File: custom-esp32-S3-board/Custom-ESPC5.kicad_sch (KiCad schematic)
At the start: 52 parts, among them J1 Screw_Terminal_01x02, J10 Barrel_Jack, J12 Conn_01x05, J13 Conn_01x05, J4 USB_C_Receptacle_USB2.0_14P, J5 Conn_01x03, J6 Screw_Terminal_01x03, SW1 SW_Nidec_CAS-120A1, SW2 SW_Push, SW3 SW_Push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

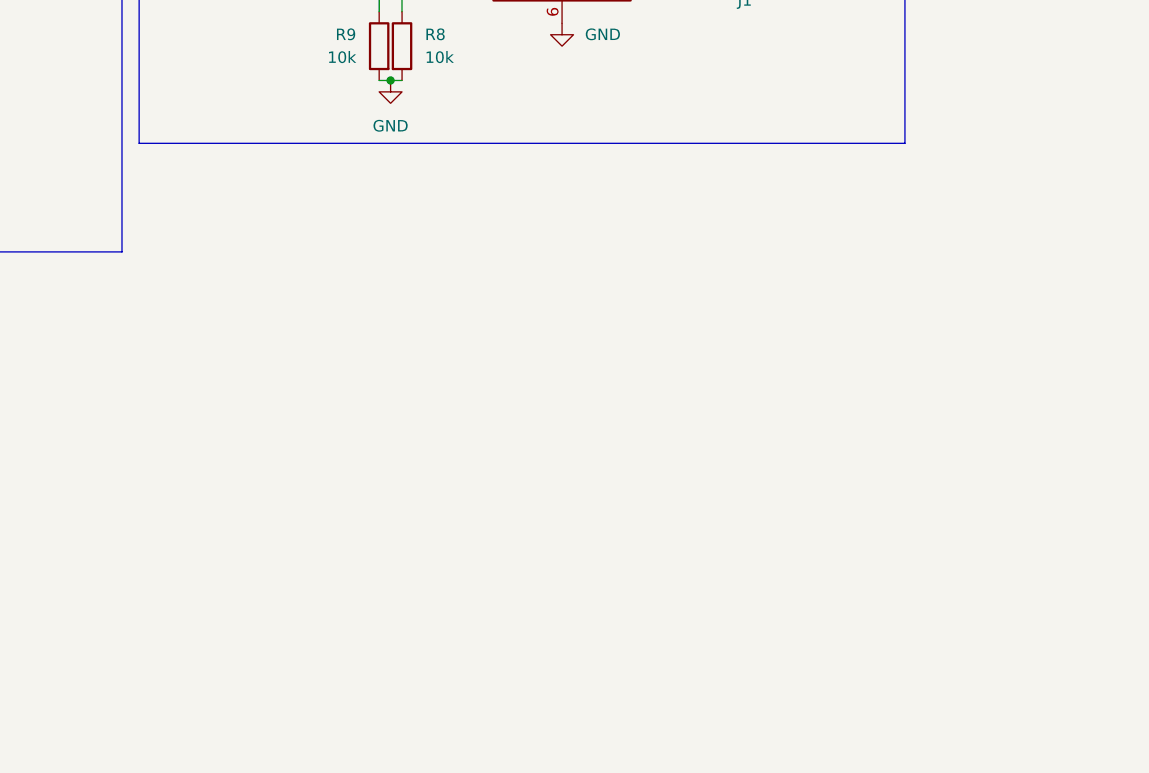
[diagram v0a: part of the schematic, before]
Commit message: add auto-reset
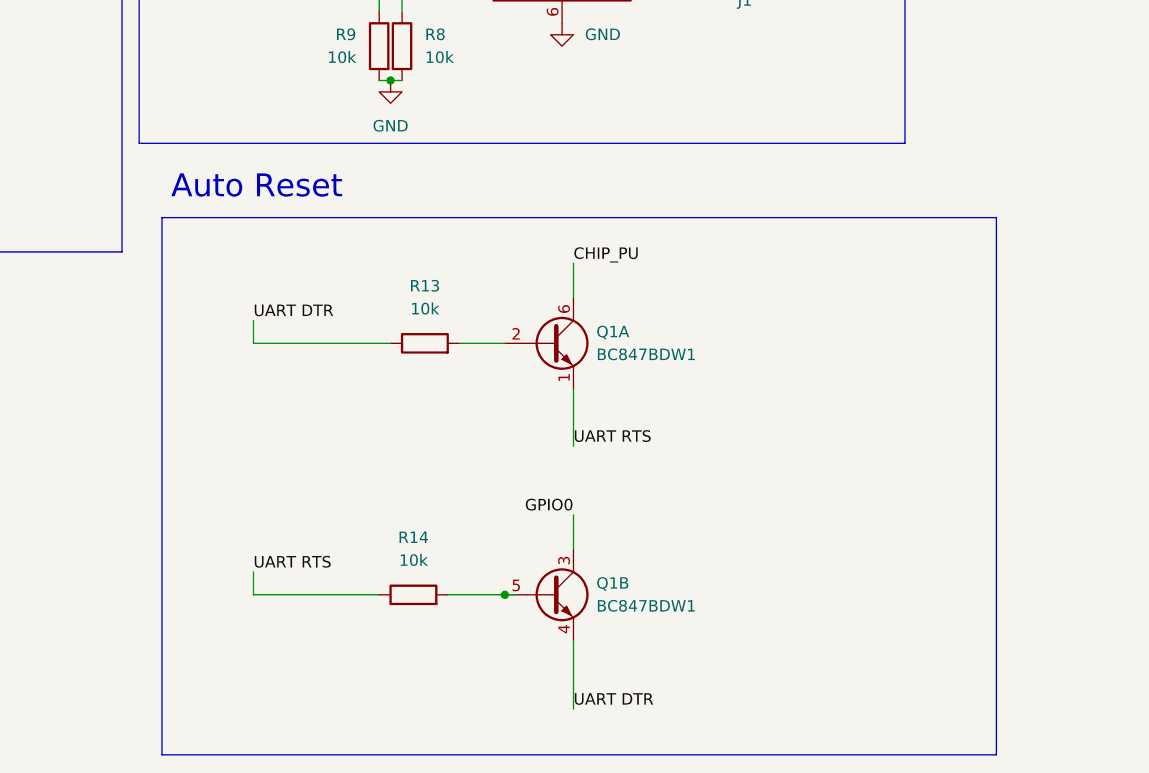
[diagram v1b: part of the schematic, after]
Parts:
- added Q1: BC847BDW1, Package_TO_SOT_SMD:SOT-363_SC-70-6, symbol Transistor_BJT:BC847BDW1
- added R13, R14: 10k, symbol Device:R
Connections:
- net CHIP_PU: now also Q1.6 (C1)
- net GPIO0: now also Q1.3 (C2)
- net UART DTR: now also Q1.4 (E2), R13.1
- net UART RTS: now also Q1.1 (E1), R14.1
- new net: Q1.5 (B2), R14.2
- new net: Q1.2 (B1), R13.2
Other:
- note added: "Auto Reset"

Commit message: Finalize Schematic
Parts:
- removed D1, D4: D, Diode_SMD:USC-TOS, symbol Device:D
- added C17, C18, C19, C20: 0.1u, Capacitor_SMD:C_0402_1005Metric, symbol Device:C
- added J2, J3, J7, J8: Conn_01x02_Pin, Connector_PinHeader_2.54mm:PinHeader_1x02_P2.54mm_Vertical, symbol Connector:Conn_01x02_Pin
- R13, R14: footprint (none) -> Resistor_SMD:R_0402_1005Metric
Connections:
- net +3.3V: no longer J5.1 (Pin_1)
- net +5V: now also J7.1 (Pin_1), J8.2 (Pin_2)
- net A1: now also C19.1
- net A2: now also C17.1
- net B1: now also C20.1
- net B2: now also C18.1
- net CHIP_PU: now also J2.1 (Pin_1); no longer Q1.6 (C1)
- net GND: now also C17.2, C18.2, C19.2, C20.2
- net GPIO0: now also J3.1 (Pin_1); no longer Q1.3 (C2)
- net at C5.1, C6.1, D2.2 (K)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: now also J7.2 (Pin_2)
- net at C2.1, R2.2, U2.2 (VO): now also J8.1 (Pin_1)
- net UART1 RX: now reaches U6.11 (IO18)
- net UART RX renamed UART0 RX
- net UART TX renamed UART0 TX
- net WS2812 renamed UART1 TX
- net UART1 TX: no longer J5.2 (Pin_2)
- new net: J3.2 (Pin_2), Q1.3 (C2)
- new net: J2.2 (Pin_2), Q1.6 (C1)
- new net UART1_RX: J5.2 (Pin_2)
- new net UART1_TX: J5.1 (Pin_1)
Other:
- note added: "Hall Effect Sensor Decoupling Caps"
- note added: "PDH Power Select"
- note added: "Shunt"
- note added: "UART JST"
- note added: "USB Power Select"
- note removed: "Forward voltage drop: 0.1 V @ 10mA 0.22V @ 100 mA 0.34 V @ 1 A"
- note removed: "WS2812 LEDs"
- moved on the sheet: Q1A, Q1B, R13, R14

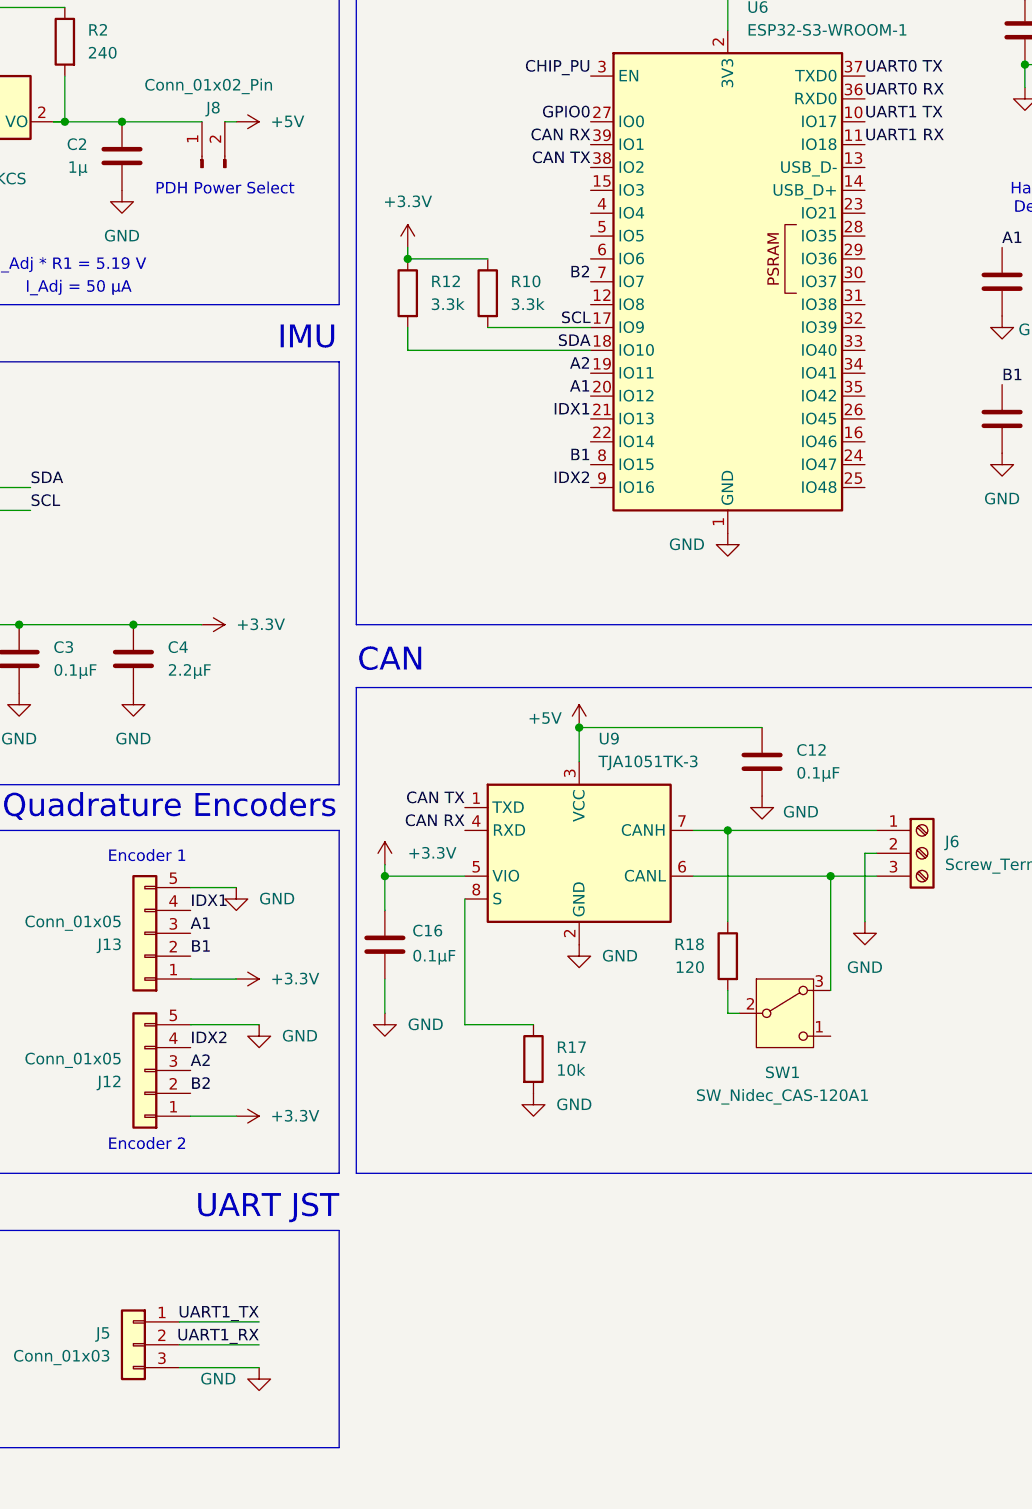
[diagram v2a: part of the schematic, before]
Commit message: Fix pin labels in schematic
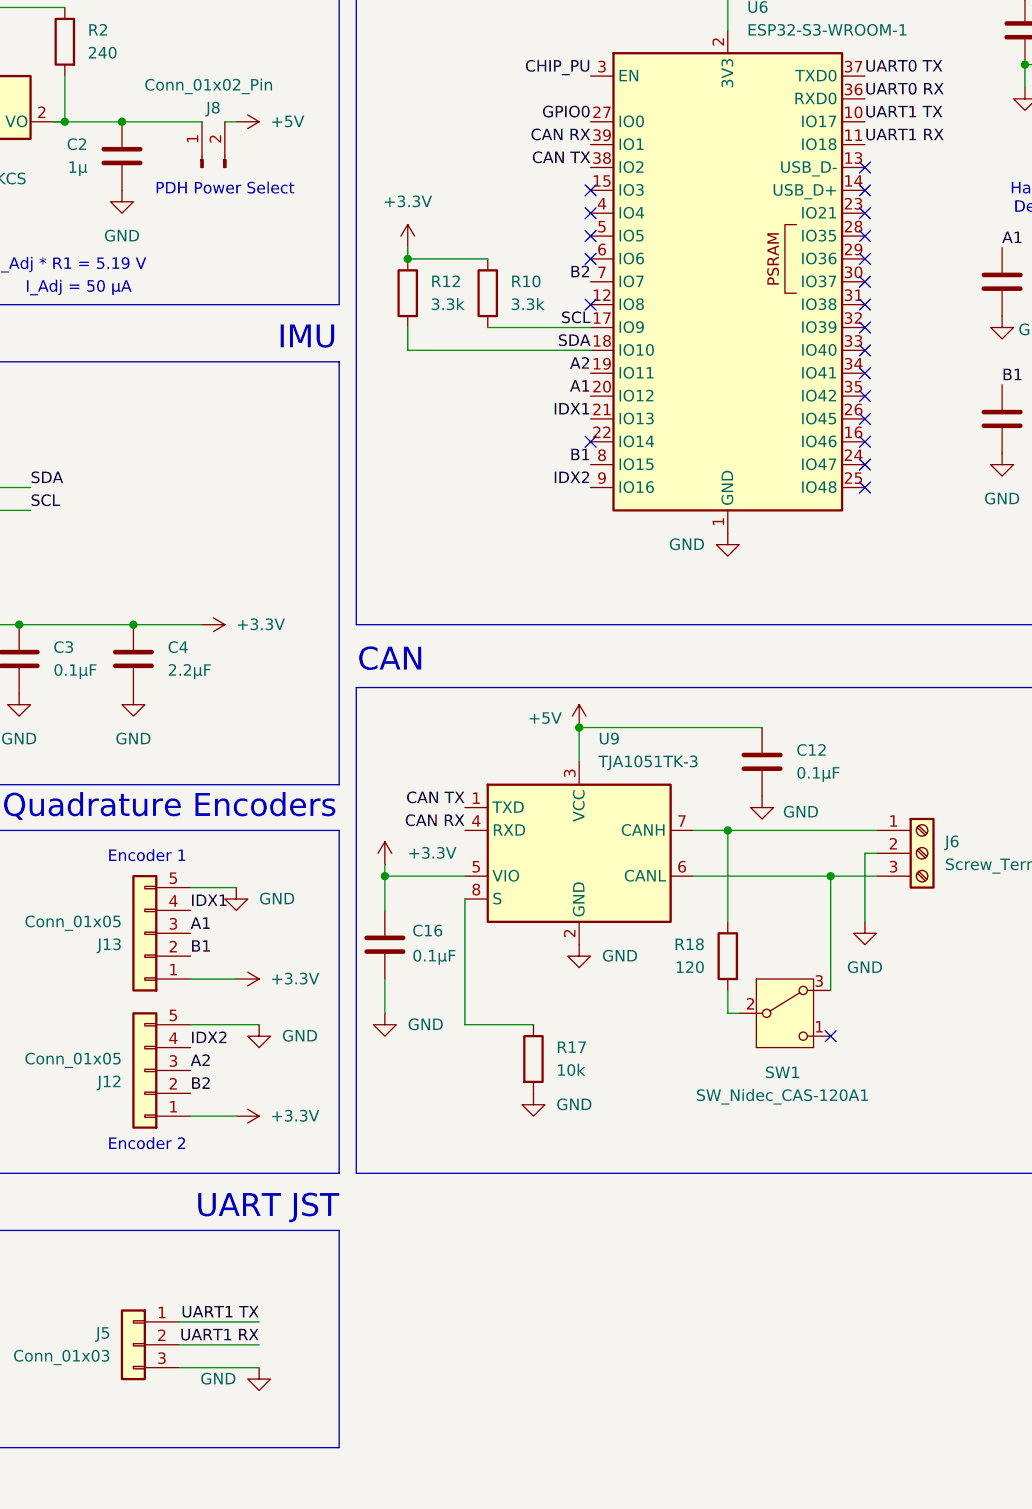
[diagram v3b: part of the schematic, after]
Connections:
- net UART1_RX is gone; now on net UART1 RX: J5.2 (Pin_2)
- net UART1_TX is gone; now on net UART1 TX: J5.1 (Pin_1)
- no-connect marks 16 -> 38
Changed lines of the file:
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@@
+	)
+	(no_connect
+		(at 596.9 387.35)
+	)
+	(no_connect
+		(at 596.9 356.87)
 	)
 	(no_connect
@@
 	)
 	(no_connect
+		(at 596.9 382.27)
+	)
+	(no_connect
 		(at 727.71 351.79)
 	)
 	(no_connect
+		(at 593.09 450.85)
+	)
+	(no_connect
+		(at 596.9 369.57)
+	)
+	(no_connect
+		(at 596.9 389.89)
+	)
+	(no_connect
 		(at 727.71 349.25)
 	)
 	(no_connect
+		(at 596.9 359.41)
+	)
+	(no_connect
+		(at 566.42 384.81)
+	)
+	(no_connect
 		(at 727.71 356.87)
 	)
@@
 	)
 	(no_connect
+		(at 596.9 364.49)
+	)
+	(no_connect
+		(at 566.42 369.57)
+	)
+	(no_connect
+		(at 566.42 356.87)
+	)
+	(no_connect
 		(at 727.71 359.41)
 	)
@@
 	)
 	(no_connect
+		(at 596.9 379.73)
+	)
+	(no_connect
+		(at 566.42 364.49)
+	)
+	(no_connect
+		(at 596.9 361.95)
+	)
+	(no_connect
+		(at 596.9 372.11)
+	)
+	(no_connect
 		(at 402.59 397.51)
 	)
 	(no_connect
+		(at 596.9 374.65)
+	)
+	(no_connect
 		(at 727.71 364.49)
 	)
 	(no_connect
+		(at 566.42 361.95)
+	)
+	(no_connect
 		(at 727.71 334.01)
 	)
 	(no_connect
 		(at 650.24 384.81)
+	)
+	(no_connect
+		(at 596.9 384.81)
+	)
+	(no_connect
+		(at 566.42 359.41)
+	)
+	(no_connect
+		(at 596.9 367.03)
+	)
+	(no_connect
+		(at 596.9 354.33)
+	)
+	(no_connect
+		(at 596.9 377.19)
 	)
 	(no_connect
@@
 		)
 	)
-	(label "UART1_TX"
+	(label "UART1 TX"
 		(at 529.59 482.6 180)
 		(effects
@@
 		)
 	)
-	(label "UART1_RX"
+	(label "UART1 RX"
 		(at 529.59 485.14 180)
 		(effects

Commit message: Finish routing for subcircuits
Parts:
- added H1, H2, H3: MountingHole, MountingHole:MountingHole_4.5mm, symbol Mechanical:MountingHole
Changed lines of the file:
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@@
 	)
 	(symbol
+		(lib_id "Mechanical:MountingHole")
+		(at 586.74 490.22 0)
+		(unit 1)
+		(exclude_from_sim no)
+		(in_bom no)
+		(on_board yes)
+		(dnp no)
+		(fields_autoplaced yes)
+		(property "Reference" "H2"
+			(at 589.28 488.9499 0)
+			(effects
+				(font
+					(size 1.27 1.27)
+				)
+				(justify left)
+			)
+		)
+		(property "Value" "MountingHole"
+			(at 589.28 491.4899 0)
+			(effects
+				(font
+					(size 1.27 1.27)
+				)
+				(justify left)
+			)
+		)
+		(property "Footprint" "MountingHole:MountingHole_4.5mm"
+			(at 586.74 490.22 0)
+			(effects
+				(font
+					(size 1.27 1.27)
+				)
+				(hide yes)
+			)
+		)
+		(property "Datasheet" "~"
+			(at 586.74 490.22 0)
+			(effects
+				(font
+					(size 1.27 1.27)
+				)
+				(hide yes)
+			)
+		)
+		(property "Description" "Mounting Hole without connection"
+			(at 586.74 490.22 0)
+			(effects
+				(font
+					(size 1.27 1.27)
+				)
+				(hide yes)
+			)
+		)
+		(instances
+			(project "Custom-ESPC5"
+				(path "/7f255074-3667-433c-aa2e-2c052ef2e2c8"
+					(reference "H2")
+					(unit 1)
+				)
+			)
+		)
+	)
+	(symbol
 		(lib_id "Device:C")
 		(at 585.47 420.37 0)
@@
 	)
 	(symbol
+		(lib_id "Mechanical:MountingHole")
+		(at 562.61 506.73 0)
+		(unit 1)
+		(exclude_from_sim no)
+		(in_bom no)
+		(on_board yes)
+		(dnp no)
+		(fields_autoplaced yes)
+		(property "Reference" "H3"
+			(at 565.15 505.4599 0)
+			(effects
+				(font
+					(size 1.27 1.27)
+				)
+				(justify left)
+			)
+		)
+		(property "Value" "MountingHole"
+			(at 565.15 507.9999 0)
+			(effects
+				(font
+					(size 1.27 1.27)
+				)
+				(justify left)
+			)
+		)
+		(property "Footprint" "MountingHole:MountingHole_4.5mm"
+			(at 562.61 506.73 0)
+			(effects
+				(font
+					(size 1.27 1.27)
+				)
+				(hide yes)
+			)
+		)
+		(property "Datasheet" "~"
+			(at 562.61 506.73 0)
+			(effects
+				(font
+					(size 1.27 1.27)
+				)
+				(hide yes)
+			)
+		)
+		(property "Description" "Mounting Hole without connection"
+			(at 562.61 506.73 0)
+			(effects
+				(font
+					(size 1.27 1.27)
+				)
+				(hide yes)
+			)
+		)
+		(instances
+			(project "Custom-ESPC5"
+				(path "/7f255074-3667-433c-aa2e-2c052ef2e2c8"
+					(reference "H3")
+					(unit 1)
+				)
+			)
+		)
+	)
+	(symbol
 		(lib_id "Regulator_Linear:LM3940")
 		(at 609.6 297.18 0)
@@
 					(unit 1)
 				)
+			)
+		)
+	)
+	(symbol
+		(lib_id "Mechanical:MountingHole")
+		(at 562.61 490.22 0)
+		(unit 1)
+		(exclude_from_sim no)
+		(in_bom no)
+		(on_board yes)
+		(dnp no)
+		(fields_autoplaced yes)
+		(property "Reference" "H1"
+			(at 565.15 488.9499 0)
+			(effects
+				(font
+					(size 1.27 1.27)
+				)
+				(justify left)
+			)
+		)
+		(property "Value" "MountingHole"
+			(at 565.15 491.4899 0)
+			(effects
+				(font
+					(size 1.27 1.27)
+				)
+				(justify left)
+			)
+		)
+		(property "Footprint" "MountingHole:MountingHole_4.5mm"
+			(at 562.61 490.22 0)
+			(effects
+				(font
+					(size 1.27 1.27)
+				)
+				(hide yes)
+			)
+		)
+		(property "Datasheet" "~"
+			(at 562.61 490.22 0)
+			(effects
+				(font
+					(size 1.27 1.27)
+				)
+				(hide yes)
+			)
+		)
+		(property "Description" "Mounting Hole without connection"
+			(at 562.61 490.22 0)
+			(effects
+				(font
+					(size 1.27 1.27)
+				)
+				(hide yes)
+			)
+		)
+		(instances
+			(project ""
+				(path "/7f255074-3667-433c-aa2e-2c052ef2e2c8"
+					(reference "H1")
+					(unit 1)
+				)

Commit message: Final Edits
Generated gerbers
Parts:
- removed R11, R16: 10k, Resistor_SMD:R_0402_1005Metric, symbol Device:R
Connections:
- net CHIP_PU: now also SW2.2
- net GND: no longer J1.2 (Pin_2), U5.7 (IN-)
- net GPIO0: now also SW3.2
- new net: J1.2 (Pin_2), U5.7 (IN-)
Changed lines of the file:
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@@
 	)
 	(junction
-		(at 689.61 433.07)
-		(diameter 0)
-		(color 0 0 0 0)
-	)
-	(junction
 		(at 678.18 420.37)
 		(diameter 0)
@@
 	(wire
 		(pts
-			(xy 574.04 304.8) (xy 574.04 303.53)
-		)
-		(stroke
-			(width 0)
-			(type default)
-		)
-	)
-	(wire
-		(pts
 			(xy 499.11 325.12) (xy 499.11 327.66)
 		)
@@
 	(wire
 		(pts
+			(xy 574.04 303.53) (xy 574.04 313.69)
+		)
+		(stroke
+			(width 0)
+			(type default)
+		)
+	)
+	(wire
+		(pts
 			(xy 654.685 330.2) (xy 654.685 328.93)
 		)
@@
 	(wire
 		(pts
-			(xy 515.62 304.8) (xy 511.81 304.8)
+			(xy 511.81 304.8) (xy 523.24 304.8)
 		)
 		(stroke
@@
 	(wire
 		(pts
-			(xy 689.61 433.07) (xy 688.34 433.07)
-		)
-		(stroke
-			(width 0)
-			(type default)
-		)
-	)
-	(wire
-		(pts
 			(xy 673.1 364.49) (xy 680.72 364.49)
 		)
@@
 	(wire
 		(pts
-			(xy 690.88 433.07) (xy 689.61 433.07)
+			(xy 688.34 433.07) (xy 690.88 433.07)
 		)
 		(stroke
@@
 	(wire
 		(pts
-			(xy 574.04 313.69) (xy 574.04 312.42)
-		)
-		(stroke
-			(width 0)
-			(type default)
-		)
-	)
-	(wire
-		(pts
 			(xy 693.42 431.8) (xy 690.88 431.8)
 		)
@@
 	)
 	(symbol
-		(lib_id "power:GND")
-		(at 689.61 433.07 0)
-		(unit 1)
-		(exclude_from_sim no)
-		(in_bom yes)
-		(on_board yes)
-		(dnp no)
-		(property "Reference" "#PWR026"
-			(at 689.61 439.42 0)
-			(effects
-				(font
-					(size 1.27 1.27)
-				)
-				(hide yes)
-			)
-		)
-		(property "Value" "GND"
-			(at 687.578 436.88 0)
-			(effects
-				(font
-					(size 1.27 1.27)
-				)
-				(justify left)
-			)
-		)
-		(property "Footprint" ""
-			(at 689.61 433.07 0)
-			(effects
-				(font
-					(size 1.27 1.27)
-				)
-				(hide yes)
-			)
-		)
-		(property "Datasheet" ""
-			(at 689.61 433.07 0)
-			(effects
-				(font
-					(size 1.27 1.27)
-				)
-				(hide yes)
-			)
-		)
-		(property "Description" "Power symbol creates a global label with name \"GND\" , ground"
-			(at 689.61 433.07 0)
-			(effects
-				(font
-					(size 1.27 1.27)
-				)
-				(hide yes)
-			)
-		)
-		(pin "1"
-		)
-		(instances
-			(project "Custom-ESPC5"
-				(path "/7f255074-3667-433c-aa2e-2c052ef2e2c8"
-					(reference "#PWR026")
-					(unit 1)
-				)
-			)
-		)
-	)
-	(symbol
 		(lib_id "Connector:Barrel_Jack")
 		(at 468.63 346.71 0)
@@
 	)
 	(symbol
-		(lib_id "Device:R")
-		(at 574.04 308.61 0)
-		(unit 1)
-		(exclude_from_sim no)
-		(in_bom yes)
-		(on_board yes)
-		(dnp no)
-		(fields_autoplaced yes)
-		(property "Reference" "R16"
-			(at 576.58 307.3399 0)
-			(effects
-				(font
-					(size 1.27 1.27)
-				)
-				(justify left)
-			)
-		)
-		(property "Value" "10k"
-			(at 576.58 309.8799 0)
-			(effects
-				(font
-					(size 1.27 1.27)
-				)
-				(justify left)
-			)
-		)
-		(property "Footprint" "Resistor_SMD:R_0402_1005Metric"
-			(at 572.262 308.61 90)
-			(effects
-				(font
-					(size 1.27 1.27)
-				)
-				(hide yes)
-			)
-		)
-		(property "Datasheet" "~"
-			(at 574.04 308.61 0)
-			(effects
-				(font
-					(size 1.27 1.27)
-				)
-				(hide yes)
-			)
-		)
-		(property "Description" "Resistor"
-			(at 574.04 308.61 0)
-			(effects
-				(font
-					(size 1.27 1.27)
-				)
-				(hide yes)
-			)
-		)
-		(pin "2"
-		)
-		(pin "1"
-		)
-		(instances
-			(project ""
-				(path "/7f255074-3667-433c-aa2e-2c052ef2e2c8"
-					(reference "R16")
-					(unit 1)
-				)
-			)
-		)
-	)
-	(symbol
 		(lib_id "power:+3.3V")
 		(at 717.55 321.31 0)
@@
 					(unit 1)
 				)
-			)
-		)
-	)
-	(symbol
-		(lib_id "Device:R")
-		(at 519.43 304.8 90)
-		(mirror x)
-		(unit 1)
-		(exclude_from_sim no)
-		(in_bom yes)
-		(on_board yes)
-		(dnp no)
-		(fields_autoplaced yes)
-		(property "Reference" "R11"
-			(at 519.43 298.45 90)
-			(effects
-				(font
-					(size 1.27 1.27)
-				)
-			)
-		)
-		(property "Value" "10k"
-			(at 519.43 300.99 90)
-			(effects
-				(font
-					(size 1.27 1.27)
-				)
-			)
-		)
-		(property "Footprint" "Resistor_SMD:R_0402_1005Metric"
-			(at 519.43 303.022 90)
-			(effects
-				(font
-					(size 1.27 1.27)
-				)
-				(hide yes)
-			)
-		)
-		(property "Datasheet" "~"
-			(at 519.43 304.8 0)
-			(effects
-				(font
-					(size 1.27 1.27)
-				)
-				(hide yes)
-			)
-		)
-		(property "Description" "Resistor"
-			(at 519.43 304.8 0)
-			(effects
-				(font
-					(size 1.27 1.27)
-				)
-				(hide yes)
-			)
-		)
-		(pin "2"
-		)
-		(pin "1"
-		)
-		(instances
-			(project "Custom-ESPC5"
-				(path "/7f255074-3667-433c-aa2e-2c052ef2e2c8"
-					(reference "R11")
-					(unit 1)
-				)

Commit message: Edit silkscreen
Increased package size of C7 :(
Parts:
- C7: footprint Capacitor_SMD:C_0402_1005Metric -> Capacitor_SMD:C_0805_2012Metric
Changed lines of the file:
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@@
 			)
 		)
-		(property "Footprint" "Capacitor_SMD:C_0402_1005Metric"
+		(property "Footprint" "Capacitor_SMD:C_0805_2012Metric"
 			(at 624.5352 307.34 0)
 			(effects
